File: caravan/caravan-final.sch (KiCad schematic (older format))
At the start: 49 parts

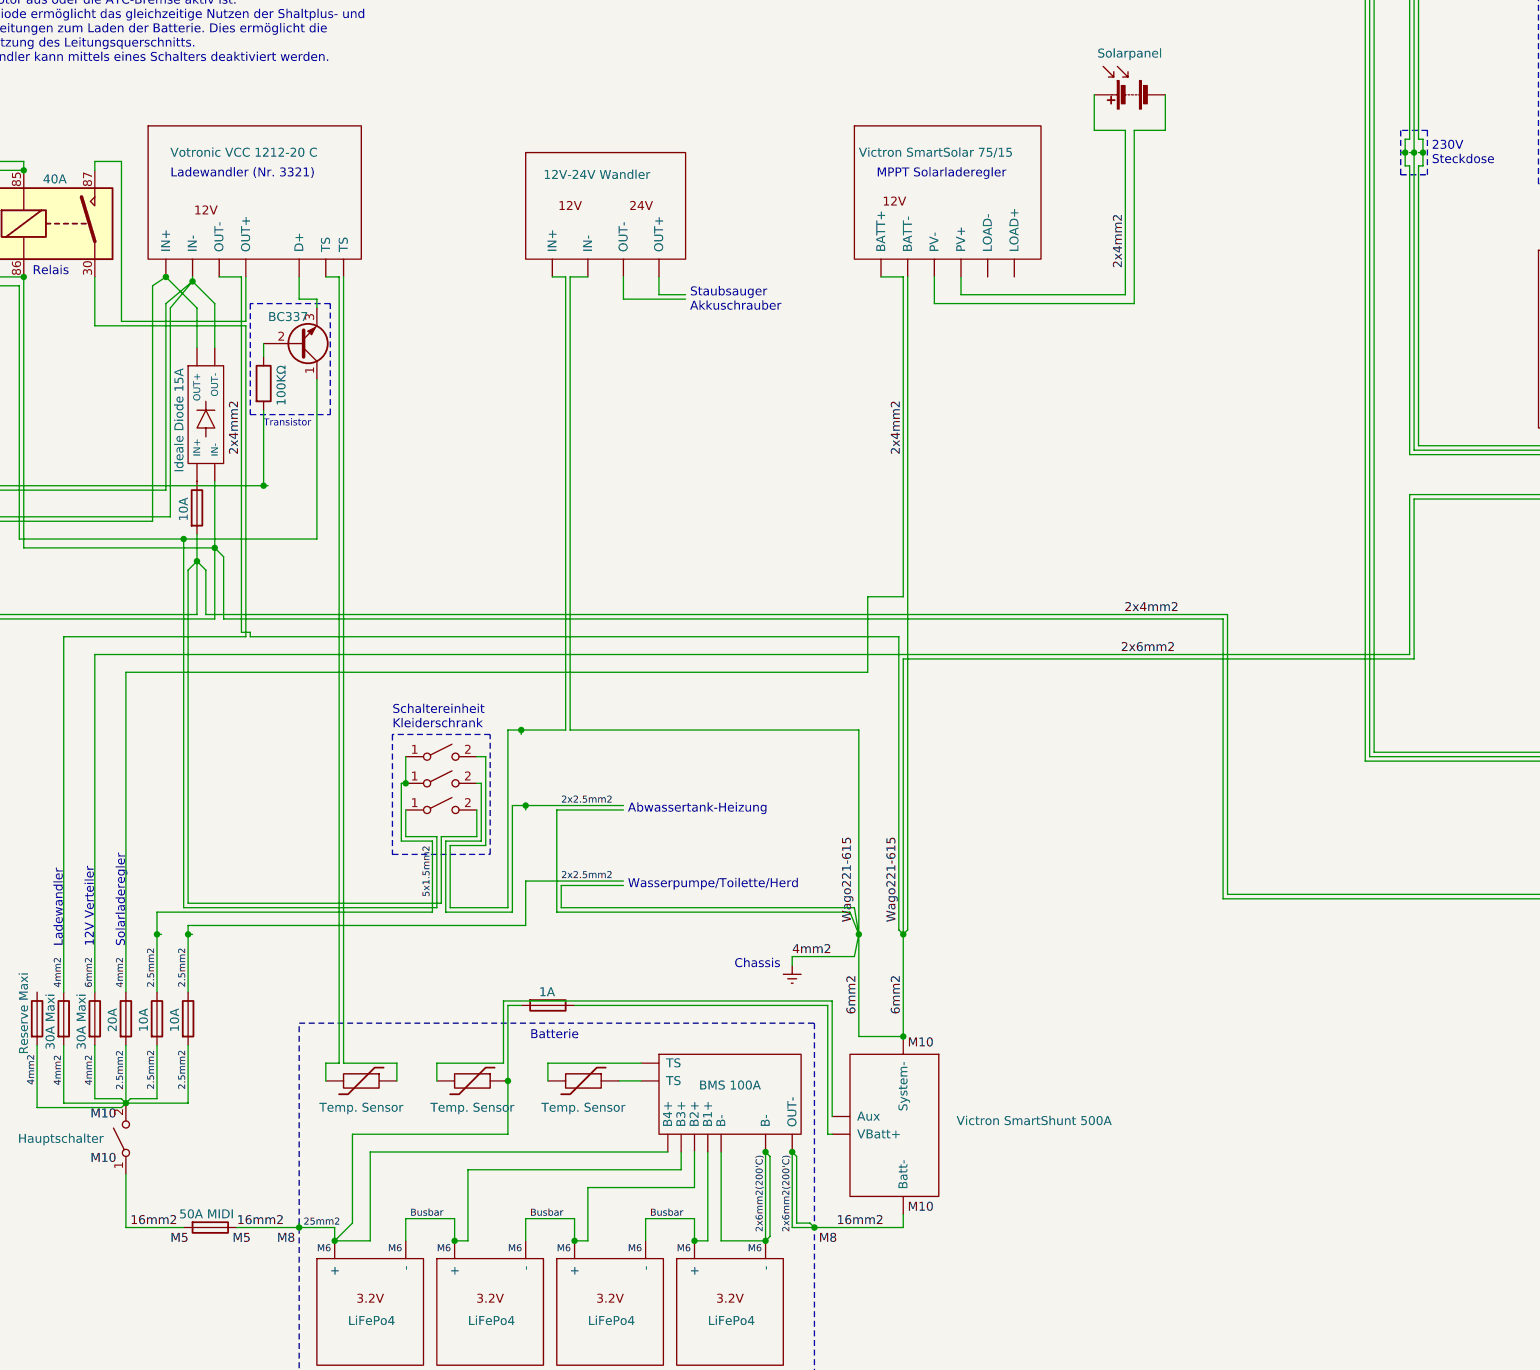
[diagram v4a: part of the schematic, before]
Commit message: caravan: Reworked negative distribution at shunt
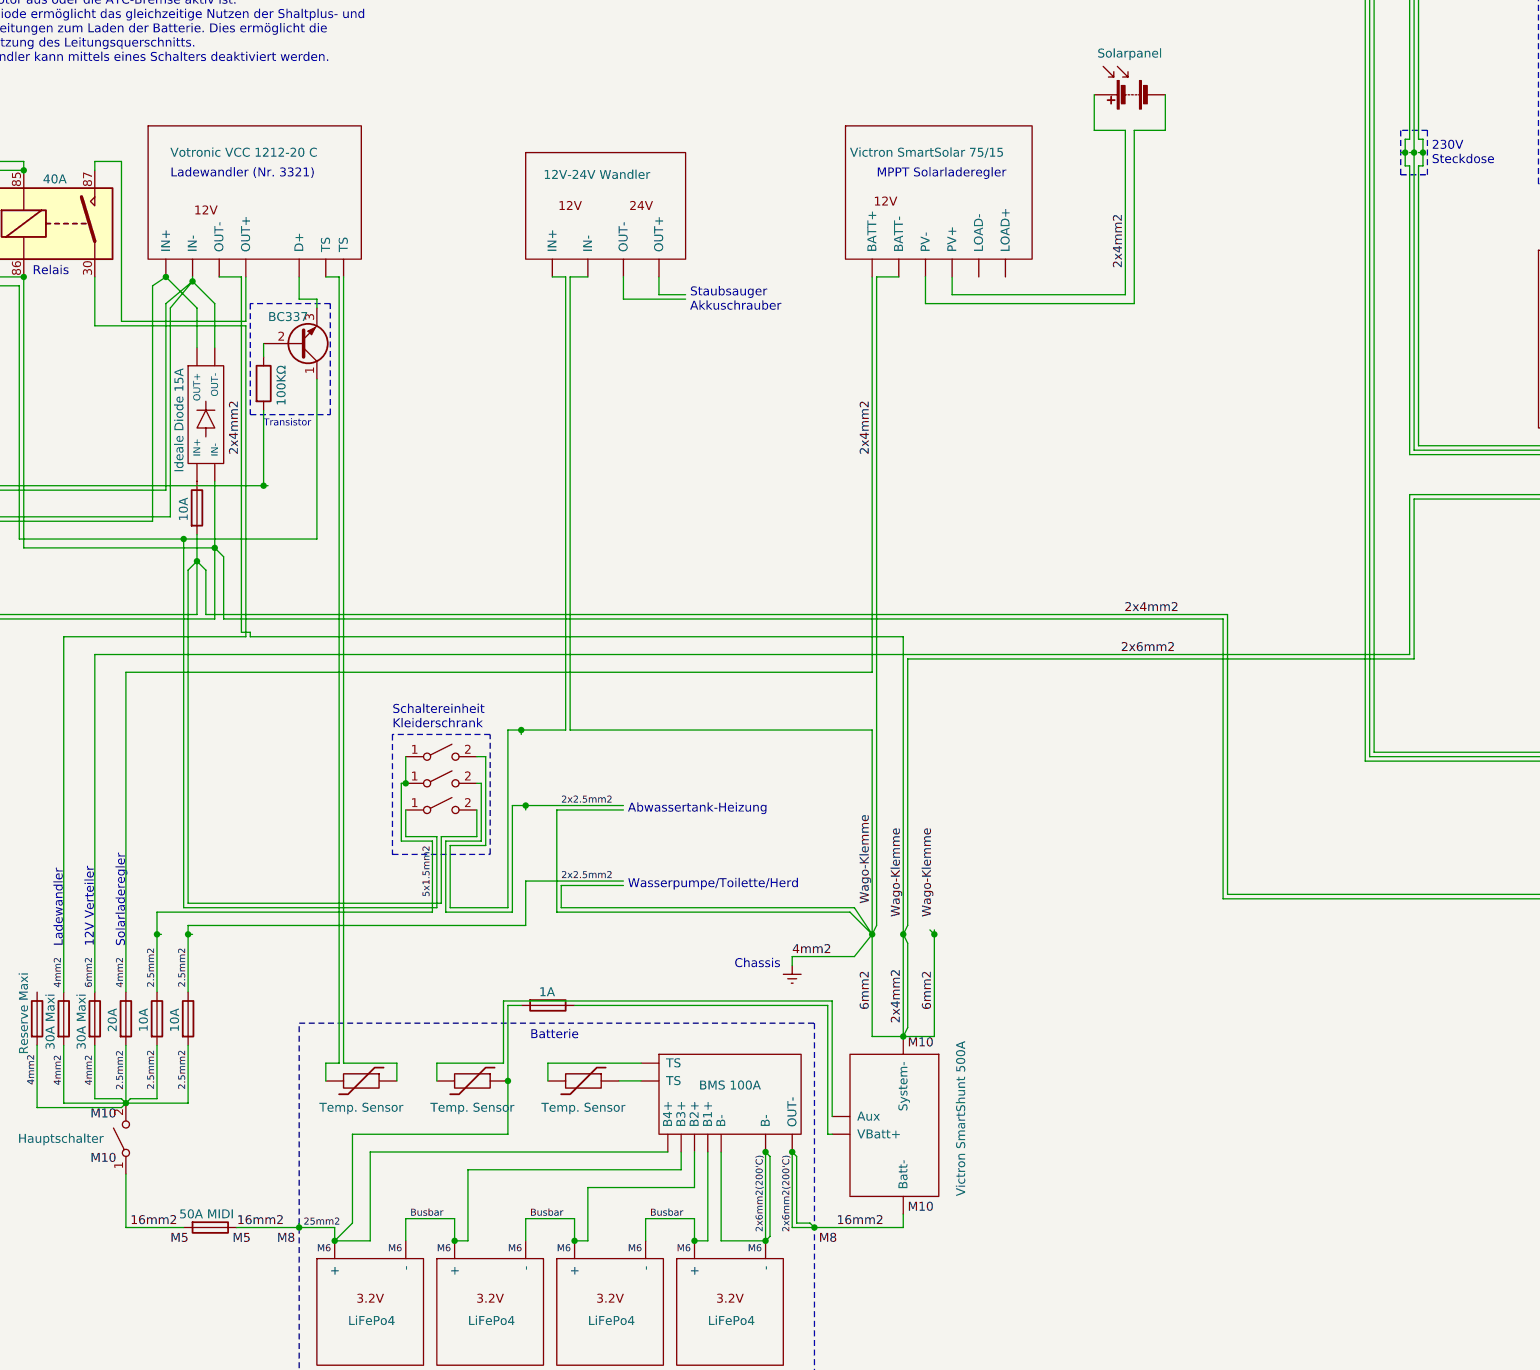
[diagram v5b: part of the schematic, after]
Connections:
- net labels added: Wago-Klemme
- net labels removed: Wago221-615
- wire segments 423 -> 428
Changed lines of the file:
@@
 	9800 3075 9800 4000
 Wire Wire Line
-	8875 4000 8875 3900
+	8825 4000 8825 3900
 Wire Wire Line
 	9850 3075 9850 4050
 Wire Wire Line
-	8725 4050 8725 3900
+	8675 4050 8675 3900
 Text Label 9800 3850 1    50   ~ 0
 2x4mm2
@@
 $EndComp
 Wire Wire Line
-	8525 7575 8550 7600
-Connection ~ 8550 7600
-Wire Wire Line
-	8575 7575 8550 7600
-Wire Wire Line
-	8275 7450 8300 7600
+	8275 7450 8375 7600
 Wire Wire Line
 	8550 9250 8550 9175
@@
 Text Label 4000 7900 1    39   ~ 0
 6mm2
-Text Label 8525 7050 3    50   ~ 0
-Wago221-615
-Text Label 8275 7050 3    50   ~ 0
-Wago221-615
+Text Label 8375 6925 3    50   ~ 0
+Wago-Klemme
 Text Label 4425 9350 0    50   ~ 0
 M5
@@
 2x2.5mm2
 Wire Wire Line
-	8550 3900 8425 3900
-Wire Wire Line
-	9800 4000 8875 4000
-Wire Wire Line
-	9850 4050 8725 4050
+	9800 4000 8825 4000
+Wire Wire Line
+	9850 4050 8675 4050
 Wire Wire Line
 	4200 8525 4175 8550
@@
 $EndComp
 Wire Wire Line
-	8300 6450 8300 7600
-Connection ~ 8300 7600
+	8375 6450 8375 7600
+Connection ~ 8375 7600
 Text Label 6450 9200 0    39   ~ 0
 Busbar
@@
 Busbar
 Wire Wire Line
-	8550 8175 8300 8175
+	8550 8175 8375 8175
 Text Label 4350 7675 3    39   ~ 0
 2.5mm2
@@
 Text Label 8175 9250 0    50   ~ 0
 16mm2
-Text Label 8300 8050 1    50   ~ 0
-6mm2
-Text Label 8550 8050 1    50   ~ 0
+Text Label 8375 8025 1    50   ~ 0
 6mm2
 Text Label 4775 9350 0    50   ~ 0
@@
 P 8650 8675
 F 0 "U?" H 8650 8675 50  0001 C CNN
-F 1 "Victron SmartShunt 500A" H 8450 8700 50  0000 R CNN
+F 1 "Victron SmartShunt 500A" V 8425 9150 50  0000 R CNN
 F 2 "" H 9200 9075 50  0001 C CNN
 F 3 "" H 9200 9075 50  0001 C CNN
@@
 	4350 7600 4375 7600
 Wire Wire Line
-	8300 7600 8250 7475
+	8375 7600 8250 7475
 Text Notes 7000 6925 0    50   ~ 0
 Abwassertank-Heizung
@@
 L microfarad-de:Victron_Solar_Charger U?
 U 1 1 60FBDCCA
-P 8825 3450
-F 0 "U?" H 8825 3750 50  0001 C CNN
-F 1 "Victron SmartSolar 75/15" H 8300 3700 50  0000 L CNN
-F 2 "" H 9375 3875 50  0001 C CNN
-F 3 "" H 9375 3875 50  0001 C CNN
-	1    8825 3450
+P 8775 3450
+F 0 "U?" H 8775 3750 50  0001 C CNN
+F 1 "Victron SmartSolar 75/15" H 8250 3700 50  0000 L CNN
+F 2 "" H 9325 3875 50  0001 C CNN
+F 3 "" H 9325 3875 50  0001 C CNN
+	1    8775 3450
 	1    0    0    -1
 $EndComp
@@
 	3300 3300 3300 3450
 Wire Wire Line
-	8275 7725 8300 7600
+	8275 7725 8375 7600
 $Comp
 L Device:Thermistor TH?
@@
 Wire Wire Line
 	8125 8000 8125 8725
-Wire Wire Line
-	8550 7600 8550 8175
 Connection ~ 8550 8175
 Wire Wire Line
 	8150 8725 8125 8725
 Wire Wire Line
-	8300 8175 8300 7600
+	8375 8175 8375 7600
 Text Label 9775 6025 0    50   ~ 0
 2x6mm2
@@
 	4700 3900 4825 3900
 Wire Wire Line
-	6675 6450 8300 6450
+	6675 6450 8375 6450
 Wire Wire Line
 	7925 7725 7925 7775
@@
 	12525 7000 12525 7250
 Wire Wire Line
-	8575 3900 8575 7575
-Wire Wire Line
 	6650 3900 6650 6450
 Wire Wire Line
@@
 Wire Wire Line
 	2625 5200 2625 5100
-Text Label 8550 4900 1    50   ~ 0
-2x4mm2
 Wire Wire Line
 	2625 5250 4425 5250
@@
 Text Notes 12400 4200 0    50   ~ 0
 20A Ladegerät
-Text Notes 8400 3350 0    50   ~ 0
-MPPT Solarladeregler
 $Comp
 L microfarad-de:Votronic_Charging_Converter U?
@@
 	4875 5900 4875 5925
 Wire Wire Line
-	4875 5925 8525 5925
-Wire Wire Line
-	8525 5925 8525 7575
+	4875 5925 8550 5925
 Text Label 4000 8450 1    39   ~ 0
 4mm2
@@
 	4175 6125 4175 7925
 Wire Wire Line
-	4175 6125 8350 6125
+	4175 6125 8375 6125
 Wire Wire Line
 	4000 6025 11400 6025
 Wire Wire Line
-	8550 6050 11425 6050
-Wire Wire Line
 	11425 6050 11425 5150
-Wire Wire Line
-	8550 6050 8550 7600
-Wire Wire Line
-	8350 6125 8350 5700
-Wire Wire Line
-	8350 5700 8550 5700
-Wire Wire Line
-	8550 5700 8550 3900
 Wire Wire Line
 	4000 8225 4000 8525
@@
 	1    0    0    -1
 $EndComp
+Text Label 8375 4900 1    50   ~ 0
+2x4mm2
+Wire Wire Line
+	8400 3900 8400 7550
+Wire Wire Line
+	8400 7550 8375 7600
+Wire Wire Line
+	8375 3900 8375 6125
+Wire Wire Line
+	8400 3900 8525 3900
+Wire Wire Line
+	8550 8175 8550 7600
+Wire Wire Line
+	8550 8175 8725 8175
+Wire Wire Line
+	8725 8175 8725 7600
+Wire Wire Line
+	8550 5925 8550 7600
+Connection ~ 8550 7600
+Text Label 8550 7000 3    50   ~ 0
+Wago-Klemme
+Text Label 8725 7000 3    50   ~ 0
+Wago-Klemme
+Wire Wire Line
+	8550 7600 8575 7650
+Wire Wire Line
+	8550 8175 8575 8125
+Wire Wire Line
+	8575 7650 8575 8125
+Text Label 8550 8100 1    50   ~ 0
+2x4mm2
+Text Notes 8400 3350 0    50   ~ 0
+MPPT Solarladeregler
+Text Label 8725 8025 1    50   ~ 0
+6mm2
+Wire Wire Line
+	8575 6050 11425 6050
+Wire Wire Line
+	8550 7600 8575 7550
+Wire Wire Line
+	8575 6050 8575 7550
+Wire Wire Line
+	8725 7600 8700 7575
+Wire Wire Line
+	8725 7600 8725 7575
+Connection ~ 8725 7600
 $EndSCHEMATC

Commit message: caravan: Minor update
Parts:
- F?: value Reserve Maxi -> 30A Maxi
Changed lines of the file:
@@
 Sheet 1 1
 Title "Autark-Schaltplan"
-Date "2022-04-26"
+Date "2022-04-28"
 Rev ""
 Comp ""
@@
 	9800 3075 9800 4000
 Wire Wire Line
-	8825 4000 8825 3900
+	8850 4000 8850 3900
 Wire Wire Line
 	9850 3075 9850 4050
 Wire Wire Line
-	8675 4050 8675 3900
+	8700 4050 8700 3900
 Text Label 9800 3850 1    50   ~ 0
 2x4mm2
@@
 $EndComp
 Wire Wire Line
-	8275 7450 8375 7600
-Wire Wire Line
-	8550 9250 8550 9175
+	8275 7450 8400 7600
+Wire Wire Line
+	8600 9250 8600 9175
 Text Label 12525 5125 0    50   ~ 0
 2x6mm2
@@
 Connection ~ 8050 9250
 Wire Wire Line
-	8050 9250 8550 9250
+	8050 9250 8600 9250
 Text Label 7925 9275 1    39   ~ 0
 2x6mm2(200'C)
@@
 Text Label 5775 9200 0    39   ~ 0
 Busbar
-Text Label 4175 8475 1    39   ~ 0
+Text Label 4175 8500 1    39   ~ 0
 2.5mm2
 Text Label 4000 7900 1    39   ~ 0
 6mm2
-Text Label 8375 6925 3    50   ~ 0
+Text Label 8400 6950 3    50   ~ 0
 Wago-Klemme
 Text Label 4425 9350 0    50   ~ 0
 M5
-Text Label 3975 8650 0    50   ~ 0
+Text Label 4000 8675 0    50   ~ 0
 M10
-Text Label 3975 8900 0    50   ~ 0
+Text Label 4000 8925 0    50   ~ 0
 M10
-Text Label 8575 9175 0    50   ~ 0
+Text Label 8600 9175 0    50   ~ 0
 M10
-Text Label 8575 8250 0    50   ~ 0
+Text Label 8600 8250 0    50   ~ 0
 M10
 Wire Wire Line
@@
 2x2.5mm2
 Wire Wire Line
-	9800 4000 8825 4000
-Wire Wire Line
-	9850 4050 8675 4050
+	9800 4000 8850 4000
+Wire Wire Line
+	9850 4050 8700 4050
 Wire Wire Line
 	4200 8525 4175 8550
@@
 $EndComp
 Wire Wire Line
-	8375 6450 8375 7600
-Connection ~ 8375 7600
+	8400 6450 8400 7600
+Connection ~ 8400 7600
 Text Label 6450 9200 0    39   ~ 0
 Busbar
@@
 Busbar
 Wire Wire Line
-	8550 8175 8375 8175
+	8600 8175 8400 8175
 Text Label 4350 7675 3    39   ~ 0
 2.5mm2
@@
 Text Label 8175 9250 0    50   ~ 0
 16mm2
-Text Label 8375 8025 1    50   ~ 0
+Text Label 8400 8025 1    50   ~ 0
 6mm2
 Text Label 4775 9350 0    50   ~ 0
@@
 L microfarad-de:Victron_SmartShunt U?
 U 1 1 60BA05A0
-P 8650 8675
-F 0 "U?" H 8650 8675 50  0001 C CNN
-F 1 "Victron SmartShunt 500A" V 8425 9150 50  0000 R CNN
-F 2 "" H 9200 9075 50  0001 C CNN
-F 3 "" H 9200 9075 50  0001 C CNN
-	1    8650 8675
+P 8700 8675
+F 0 "U?" H 8700 8675 50  0001 C CNN
+F 1 "Victron SmartShunt 500A" V 8475 9150 50  0000 R CNN
+F 2 "" H 9250 9075 50  0001 C CNN
+F 3 "" H 9250 9075 50  0001 C CNN
+	1    8700 8675
 	-1   0    0    -1
 $EndComp
@@
 	4350 7600 4375 7600
 Wire Wire Line
-	8375 7600 8250 7475
+	8400 7600 8250 7475
 Text Notes 7000 6925 0    50   ~ 0
 Abwassertank-Heizung
@@
 L microfarad-de:Victron_Solar_Charger U?
 U 1 1 60FBDCCA
-P 8775 3450
-F 0 "U?" H 8775 3750 50  0001 C CNN
-F 1 "Victron SmartSolar 75/15" H 8250 3700 50  0000 L CNN
-F 2 "" H 9325 3875 50  0001 C CNN
-F 3 "" H 9325 3875 50  0001 C CNN
-	1    8775 3450
+P 8800 3450
+F 0 "U?" H 8800 3750 50  0001 C CNN
+F 1 "Victron SmartSolar 75/15" H 8275 3700 50  0000 L CNN
+F 2 "" H 9350 3875 50  0001 C CNN
+F 3 "" H 9350 3875 50  0001 C CNN
+	1    8800 3450
 	1    0    0    -1
 $EndComp
@@
 	3300 3300 3300 3450
 Wire Wire Line
-	8275 7725 8375 7600
+	8275 7725 8400 7600
 $Comp
 L Device:Thermistor TH?
@@
 	6325 8000 6400 8000
 Wire Wire Line
-	6700 8000 8125 8000
+	6700 8000 8175 8000
 Wire Wire Line
 	6325 8725 6325 8425
@@
 	6300 8325 6300 7975
 Wire Wire Line
-	6300 7975 8150 7975
-Wire Wire Line
-	8150 7975 8150 8625
-Wire Wire Line
-	8125 8000 8125 8725
-Connection ~ 8550 8175
-Wire Wire Line
-	8150 8725 8125 8725
-Wire Wire Line
-	8375 8175 8375 7600
+	6300 7975 8200 7975
+Wire Wire Line
+	8200 7975 8200 8625
+Wire Wire Line
+	8175 8000 8175 8725
+Connection ~ 8600 8175
+Wire Wire Line
+	8200 8725 8175 8725
+Wire Wire Line
+	8400 8175 8400 7600
 Text Label 9775 6025 0    50   ~ 0
 2x6mm2
@@
 	4700 3900 4825 3900
 Wire Wire Line
-	6675 6450 8375 6450
+	6675 6450 8400 6450
 Wire Wire Line
 	7925 7725 7925 7775
@@
 	4875 5900 4875 5925
 Wire Wire Line
-	4875 5925 8550 5925
+	4875 5925 8525 5925
 Text Label 4000 8450 1    39   ~ 0
 4mm2
@@
 4mm2
 Wire Wire Line
-	4000 6025 4000 7925
-Wire Wire Line
 	4175 8225 4175 8550
-Wire Wire Line
-	4175 6125 4175 7925
-Wire Wire Line
-	4175 6125 8375 6125
-Wire Wire Line
-	4000 6025 11400 6025
 Wire Wire Line
 	11425 6050 11425 5150
@@
 P 3675 8075
 F 0 "F?" H 3735 8121 50  0001 L CNN
-F 1 "Reserve Maxi" V 3600 7875 50  0000 L CNN
+F 1 "30A Maxi" V 3600 7900 50  0000 L CNN
 F 2 "" V 3605 8075 50  0001 C CNN
 F 3 "~" H 3675 8075 50  0001 C CNN
@@
 	1    0    0    -1
 $EndComp
-Text Label 8375 4900 1    50   ~ 0
+Text Label 8400 4900 1    50   ~ 0
 2x4mm2
 Wire Wire Line
-	8400 3900 8400 7550
-Wire Wire Line
-	8400 7550 8375 7600
-Wire Wire Line
-	8375 3900 8375 6125
-Wire Wire Line
-	8400 3900 8525 3900
-Wire Wire Line
-	8550 8175 8550 7600
-Wire Wire Line
-	8550 8175 8725 8175
-Wire Wire Line
-	8725 8175 8725 7600
-Wire Wire Line
-	8550 5925 8550 7600
-Connection ~ 8550 7600
-Text Label 8550 7000 3    50   ~ 0
+	8600 8175 8800 8175
+Wire Wire Line
+	8800 8175 8800 7600
+Text Label 8800 7025 3    50   ~ 0
 Wago-Klemme
-Text Label 8725 7000 3    50   ~ 0
-Wago-Klemme
-Wire Wire Line
-	8550 7600 8575 7650
-Wire Wire Line
-	8550 8175 8575 8125
-Wire Wire Line
-	8575 7650 8575 8125
-Text Label 8550 8100 1    50   ~ 0
-2x4mm2
+Wire Wire Line
+	8600 8175 8675 8100
 Text Notes 8400 3350 0    50   ~ 0
 MPPT Solarladeregler
-Text Label 8725 8025 1    50   ~ 0
+Text Label 8800 8025 1    50   ~ 0
 6mm2
 Wire Wire Line
-	8575 6050 11425 6050
-Wire Wire Line
-	8550 7600 8575 7550
-Wire Wire Line
-	8575 6050 8575 7550
-Wire Wire Line
-	8725 7600 8700 7575
-Wire Wire Line
-	8725 7600 8725 7575
-Connection ~ 8725 7600
+	8675 6050 11425 6050
+Wire Wire Line
+	8800 7600 8850 7600
+Wire Wire Line
+	8800 7600 8825 7575
+Connection ~ 8800 7600
+Wire Wire Line
+	8675 6050 8675 8100
+Text Label 8675 8025 1    50   ~ 0
+6mm2
+Text Label 8525 8025 1    50   ~ 0
+4mm2
+Wire Wire Line
+	8400 3900 8400 6125
+Wire Wire Line
+	3675 7600 3675 7625
+Wire Wire Line
+	3675 7625 3700 7625
+Connection ~ 3675 7625
+Wire Wire Line
+	3675 7625 3675 7925
+Text Label 3675 7050 3    50   ~ 0
+Wago-Klemme
+Text Label 3675 7900 1    39   ~ 0
+4mm2
+Wire Wire Line
+	8400 7600 8425 7525
+Wire Wire Line
+	8425 7525 8425 3900
+Wire Wire Line
+	8425 3900 8550 3900
+Wire Wire Line
+	4000 6025 11400 6025
+Wire Wire Line
+	4175 7925 4175 6125
+Wire Wire Line
+	4175 6125 8400 6125
+Wire Wire Line
+	4000 6025 4000 7925
+Wire Wire Line
+	8525 5925 8525 8100
+Wire Wire Line
+	8525 8100 8600 8175
 $EndSCHEMATC

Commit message: Updated caravan
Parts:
- removed F? (x2): 30A Maxi, symbol Device:Fuse
- removed F?: 20A, symbol Device:Fuse
- added F? (x3): 30A MIDI, symbol Device:Fuse
- added F?: 10A, symbol Device:Fuse
- F?: value 50A MIDI -> 100A MEGA
- F?: value 30A Maxi -> 30A MIDI
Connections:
- net labels removed: Wago-Klemme
- wire segments 428 -> 426
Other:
- note added: "12V-Steckdosen Kreis 1"
- note added: "12V-Steckdosen Kreis 2"
- note added: "12V-Verteiler"
- note added: "230V-Steckdosen"
- note added: "230V-Verteiler"
- note added: "230V-\nSteckdose"
- note added: "Batterie-Verteiler"
- note added: "Reserve"
- note added: "Truma-C4-Steuerung"
- note removed: "12V Steckdosen Kreis 1"
- note removed: "12V Steckdosen Kreis 2"
- note removed: "12V Verteiler"
- note removed: "230V Steckdosen"
- note removed: "230V Verteiler"
- note removed: "230V\nSteckdose"
- note removed: "Truma C4 Steuerung"

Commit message: Updated caravan
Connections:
- net labels removed: 16mm2
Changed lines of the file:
@@
 $EndComp
 Text Label 8600 9400 1    39   ~ 0
-16mm2
+25mm2
 Text Label 8400 8025 1    50   ~ 0
 6mm2
@@
 	8600 9175 8600 9475
 Text Label 8275 9225 3    39   ~ 0
-16mm2
+25mm2
 $Comp
 L Device:Fuse F?
@@
 Connection ~ 5150 9250
 Text Label 4725 9250 0    39   ~ 0
-16mm2
+25mm2
 Wire Wire Line
 	4275 8375 4275 8700
